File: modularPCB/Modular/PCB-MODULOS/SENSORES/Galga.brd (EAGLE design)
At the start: 19 x 22 mm, 5 parts

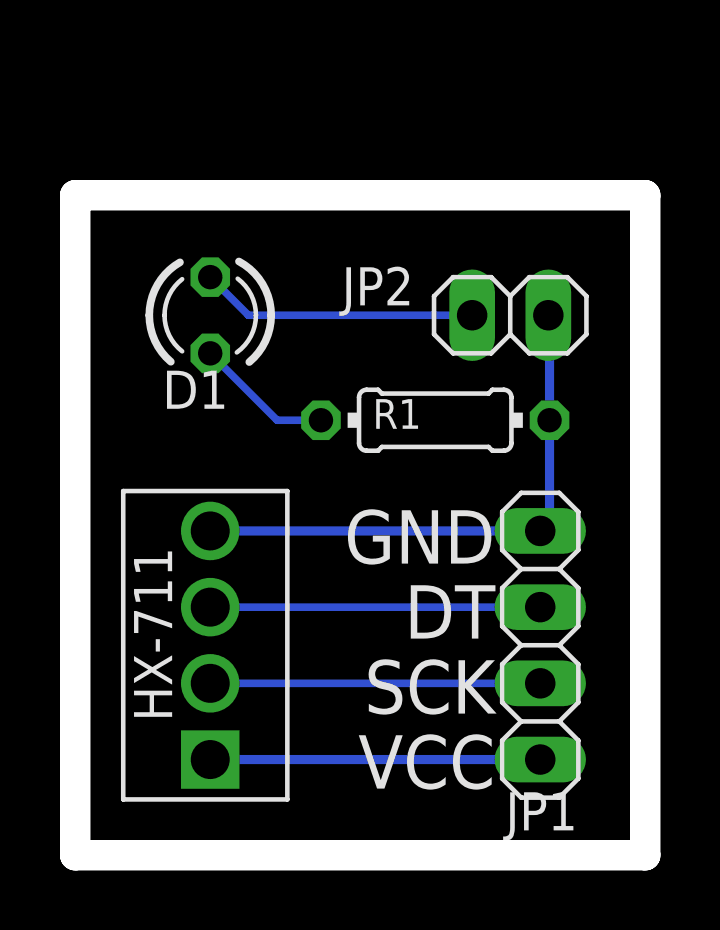
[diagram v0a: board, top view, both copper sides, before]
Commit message: Se agregaron brd de la ultima actualización
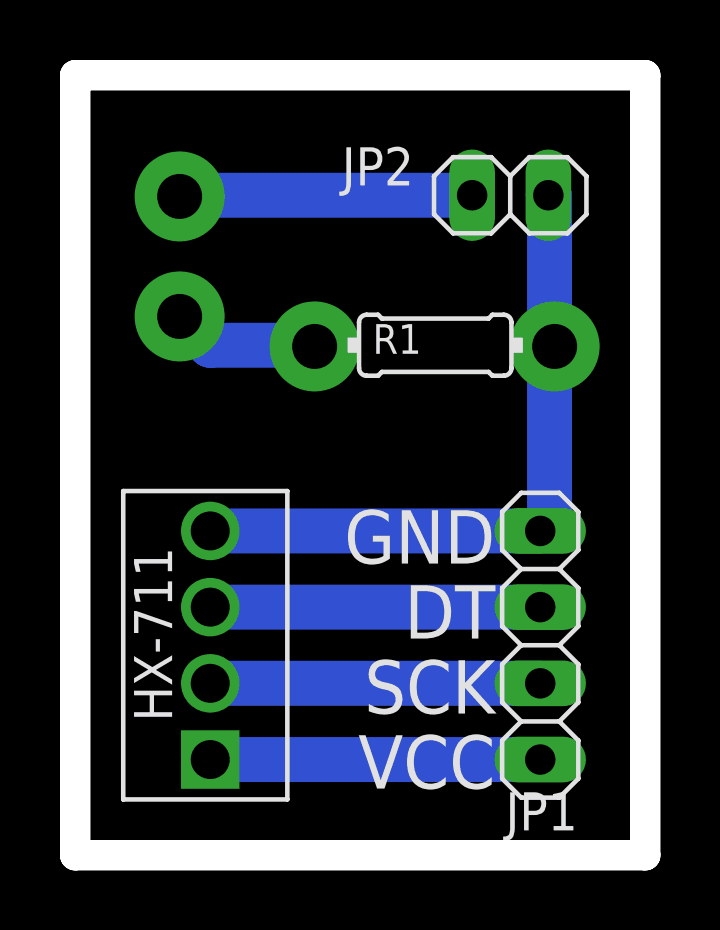
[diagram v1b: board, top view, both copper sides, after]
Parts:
- removed D1: (no value), led:LED3MM
- moved JP2 4.00 mm to (14.5, 22.0)
- moved R1 2.50 mm to (12.0, 17.0)
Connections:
- net N$8: no longer D1.K
- net PULSO-GALGA: no longer D1.A
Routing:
- net GND: track 18.3 -> 22.3 mm
- net PULSO-GALGA: track 9.26 -> 9.77 mm, vias 0 -> 3
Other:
- board size 19 x 22 mm -> 19 x 26 mm
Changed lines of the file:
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@@
 <setting verticaltext="up"/>
 </settings>
-<grid distance="0.5" unitdist="mm" unit="mm" style="lines" multiple="1" display="yes" altdistance="5" altunitdist="mil" altunit="mil"/>
+<grid distance="0.500000001" unitdist="mm" unit="mm" style="lines" multiple="1" display="yes" altdistance="5" altunitdist="mil" altunit="mil"/>
 <layers>
 <layer number="1" name="Top" color="4" fill="1" visible="yes" active="yes"/>
@@
 <plain>
 <wire x1="0" y1="0" x2="19" y2="0" width="1.016" layer="20"/>
-<wire x1="19" y1="0" x2="19" y2="22" width="1.016" layer="20"/>
-<wire x1="19" y1="22" x2="0" y2="22" width="1.016" layer="20"/>
-<wire x1="0" y1="22" x2="0" y2="0" width="1.016" layer="20"/>
+<wire x1="19" y1="0" x2="19" y2="26" width="1.016" layer="20"/>
+<wire x1="19" y1="26" x2="0" y2="26" width="1.016" layer="20"/>
+<wire x1="0" y1="26" x2="0" y2="0" width="1.016" layer="20"/>
 <text x="14" y="4" size="1.778" layer="21" rot="R180">VCC</text>
 <text x="14" y="6.5" size="1.778" layer="21" rot="R180">SCK</text>
 <text x="14" y="9" size="1.778" layer="21" rot="R180">DT</text>
 <text x="14" y="11.5" size="1.778" layer="21" rot="R180">GND</text>
-<dimension x1="19" y1="22" x2="0" y2="22" x3="9.5" y3="25" textsize="1.778" layer="48"/>
-<dimension x1="19" y1="0" x2="19" y2="22" x3="22" y3="11" textsize="1.778" layer="48" dtype="horizontal"/>
+<dimension x1="19" y1="26" x2="0" y2="26" x3="9.5" y3="27" textsize="1.778" layer="48"/>
+<dimension x1="19" y1="0" x2="19" y2="26" x3="22" y3="13" textsize="1.778" layer="48" dtype="horizontal"/>
 </plain>
 <attributes>
@@
 <attribute name="VALUE" x="12.325" y="12.08" size="1.27" layer="27" rot="R270"/>
 </element>
-<element name="JP2" library="pinhead" library_urn="urn:adsk.eagle:library:325" package="1X02" package3d_urn="urn:adsk.eagle:package:22435/2" value="" x="14.5" y="18" smashed="yes">
-<attribute name="NAME" x="8.8838" y="18.3288" size="1.27" layer="25" ratio="10"/>
-<attribute name="POPULARITY" value="98" x="31.01" y="0.22" size="1.778" layer="27" display="off"/>
-<attribute name="VALUE" x="11.96" y="14.825" size="1.27" layer="27"/>
+<element name="JP2" library="pinhead" library_urn="urn:adsk.eagle:library:325" package="1X02" package3d_urn="urn:adsk.eagle:package:22435/2" value="" x="14.5" y="22" smashed="yes">
+<attribute name="NAME" x="8.8838" y="22.3288" size="1.27" layer="25" ratio="10"/>
+<attribute name="POPULARITY" value="98" x="31.01" y="4.22" size="1.778" layer="27" display="off"/>
+<attribute name="VALUE" x="11.96" y="18.825" size="1.27" layer="27"/>
 </element>
-<element name="D1" library="led" library_urn="urn:adsk.eagle:library:259" package="LED3MM" package3d_urn="urn:adsk.eagle:package:15797/1" value="" x="4.5" y="18" smashed="yes" rot="R270">
-<attribute name="NAME" x="2.905" y="14.881" size="1.27" layer="25" ratio="10"/>
-<attribute name="POPULARITY" value="97" x="-13.28" y="-8.67" size="1.778" layer="27" rot="R270" display="off"/>
-<attribute name="VALUE" x="2.849" y="16.095" size="1.27" layer="27" ratio="10" rot="R270"/>
-</element>
-<element name="R1" library="rcl" library_urn="urn:adsk.eagle:library:334" package="0204/7" package3d_urn="urn:adsk.eagle:package:23498/2" value="220" x="12" y="14.5" smashed="yes" rot="R180">
-<attribute name="NAME" x="11.54" y="15.2046" size="0.9906" layer="25" ratio="10" rot="R180"/>
-<attribute name="POPULARITY" value="79" x="-5.78" y="37.36" size="1.778" layer="27" rot="R180" display="off"/>
-<attribute name="SPICEPREFIX" value="R" x="-5.78" y="37.36" size="1.778" layer="27" rot="R180" display="off"/>
-<attribute name="VALUE" x="14.1256" y="14.9826" size="0.9906" layer="27" ratio="10" rot="R180"/>
+<element name="R1" library="rcl" library_urn="urn:adsk.eagle:library:334" package="0204/7" package3d_urn="urn:adsk.eagle:package:23498/2" value="220" x="12" y="17" smashed="yes" rot="R180">
+<attribute name="NAME" x="11.54" y="17.7046" size="0.9906" layer="25" ratio="10" rot="R180"/>
+<attribute name="POPULARITY" value="79" x="-5.78" y="39.86" size="1.778" layer="27" rot="R180" display="off"/>
+<attribute name="SPICEPREFIX" value="R" x="-5.78" y="39.86" size="1.778" layer="27" rot="R180" display="off"/>
+<attribute name="VALUE" x="14.1256" y="17.4826" size="0.9906" layer="27" ratio="10" rot="R180"/>
 </element>
 <element name="U$2" library="MODULAR" package="HX-711" value="HX-711" x="4.5" y="7" smashed="yes" rot="R90"/>
@@
 <contactref element="U$2" pad="VCC"/>
 <contactref element="JP1" pad="4"/>
-<wire x1="4.5" y1="3.19" x2="15.5" y2="3.19" width="0.3048" layer="16"/>
+<wire x1="4.5" y1="3.19" x2="15.5" y2="3.19" width="1.5" layer="16"/>
 </signal>
 <signal name="GND">
@@
 <contactref element="R1" pad="1"/>
 <contactref element="JP2" pad="2"/>
-<wire x1="4.5" y1="10.81" x2="15.5" y2="10.81" width="0.3048" layer="16"/>
-<wire x1="15.77" y1="18" x2="15.81" y2="17.96" width="0.3048" layer="16"/>
-<wire x1="15.81" y1="17.96" x2="15.81" y2="14.5" width="0.3048" layer="16"/>
-<wire x1="15.5" y1="10.81" x2="15.81" y2="11.12" width="0.3048" layer="16"/>
-<wire x1="15.81" y1="11.12" x2="15.81" y2="14.5" width="0.3048" layer="16"/>
+<wire x1="4.5" y1="10.81" x2="15.5" y2="10.81" width="1.5" layer="16"/>
+<wire x1="15.77" y1="22" x2="15.81" y2="21.96" width="1.5" layer="16"/>
+<wire x1="15.81" y1="21.96" x2="15.81" y2="17" width="1.5" layer="16"/>
+<wire x1="15.5" y1="10.81" x2="15.81" y2="11.12" width="1.5" layer="16"/>
+<wire x1="15.81" y1="11.12" x2="15.81" y2="17" width="1.5" layer="16"/>
 </signal>
 <signal name="DT-GALGA">
 <contactref element="U$2" pad="DT"/>
 <contactref element="JP1" pad="2"/>
-<wire x1="4.5" y1="8.27" x2="15.5" y2="8.27" width="0.254" layer="16"/>
+<wire x1="4.5" y1="8.27" x2="15.5" y2="8.27" width="1.5" layer="16"/>
 </signal>
 <signal name="SCK-GALGA">
 <contactref element="U$2" pad="SCK"/>
 <contactref element="JP1" pad="3"/>
-<wire x1="4.5" y1="5.73" x2="15.5" y2="5.73" width="0.254" layer="16"/>
+<wire x1="4.5" y1="5.73" x2="15.5" y2="5.73" width="1.5" layer="16"/>
 </signal>
 <signal name="N$8">
-<contactref element="D1" pad="K"/>
 <contactref element="R1" pad="2"/>
-<wire x1="4.5" y1="16.73" x2="6.73" y2="14.5" width="0.254" layer="16"/>
-<wire x1="6.73" y1="14.5" x2="8.19" y2="14.5" width="0.254" layer="16"/>
+<wire x1="8.19" y1="17" x2="4.5" y2="17" width="1.5" layer="16"/>
+<wire x1="4.5" y1="17" x2="3.5" y2="18" width="1.5" layer="16"/>
 </signal>
 <signal name="PULSO-GALGA">
-<contactref element="D1" pad="A"/>
 <contactref element="JP2" pad="1"/>
-<wire x1="13.23" y1="18" x2="5.77" y2="18" width="0.254" layer="16"/>
-<wire x1="5.77" y1="18" x2="4.5" y2="19.27" width="0.254" layer="16"/>
+<via x="7.98" y="16.96" extent="1-16" drill="1.5" diameter="3"/>
+<via x="3.48" y="17.96" extent="1-16" drill="1.5" diameter="3"/>
+<via x="3.48" y="21.96" extent="1-16" drill="1.5" diameter="3"/>
+<wire x1="3.48" y1="21.96" x2="3.52" y2="22" width="1.5" layer="16"/>
+<wire x1="3.52" y1="22" x2="13.23" y2="22" width="1.5" layer="16"/>
+<wire x1="3.48" y1="17.96" x2="7.98" y2="16.96" width="0" layer="19" extent="1-1"/>
+<wire x1="3.48" y1="21.96" x2="3.48" y2="17.96" width="0" layer="19" extent="1-1"/>
+</signal>
+<signal name="N$4">
+<via x="15.98" y="16.96" extent="1-16" drill="1.5" diameter="3"/>
 </signal>
 </signals>
